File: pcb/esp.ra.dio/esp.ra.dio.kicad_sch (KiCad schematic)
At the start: 26 parts, among them J1 A, J10 UART, J2 B, J3 C, J4 D, J5 START, J6 SELECT, J7 JOY, J8 USB_B_Micro, J9 BATTERY, SW1 RESET, SW2 POWER, SW3 BOOT, U2 ESP32-C3-WROOM-02, U3 TLV75533PDBV

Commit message: Routing checkpoint
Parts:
- C1, C2, C3: footprint (none) -> Capacitor_SMD:C_0805_2012Metric_Pad1.18x1.45mm_HandSolder
- H1, H2, H3, H4: footprint (none) -> MountingHole:MountingHole_2.2mm_M2
- J10: footprint (none) -> Connector_PinHeader_2.54mm:PinHeader_1x04_P2.54mm_Vertical
- J8: footprint Connector_USB:USB_Micro-B_Amphenol_10118193-0001LF_Horizontal -> Connector_USB:USB_Micro-AB_Molex_47590-0001
- R1, R2, R3: footprint (none) -> Resistor_SMD:R_0805_2012Metric_Pad1.20x1.40mm_HandSolder
- SW1, SW3: footprint (none) -> Button_Switch_SMD:SW_SPST_PTS810
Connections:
- net GND: now also SW1.2; no longer SW1.1
- net VBAT: now also D2.1; no longer D2.2
- net VBUS: now also D2.2; no longer D2.1
- net VIN: now reaches SW2.2 (B), U3.1 (IN), U3.3 (EN)
- net at C3.2, R3.1: now also SW1.1; no longer SW1.2
- net VBATBUS: now reaches D2.3, SW2.3 (C)
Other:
- title: NG2040 Controller -> ESP.Ra.Dio BTLE Joystick
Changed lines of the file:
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@@
 	(paper "A4")
 	(title_block
-		(title "NG2040 Controller")
-		(date "2024-09-05")
-		(rev "4")
+		(title "ESP.Ra.Dio BTLE Joystick")
+		(date "2026-03-07")
+		(rev "2")
 		(company "@partlyhuman")
 	)
@@
 	(wire
 		(pts
+			(xy 57.15 26.67) (xy 67.31 26.67)
+		)
+		(stroke
+			(width 0)
+			(type default)
+		)
+	)
+	(wire
+		(pts
 			(xy 36.83 77.47) (xy 36.83 83.82)
 		)
@@
 	(wire
 		(pts
-			(xy 57.15 26.67) (xy 67.31 26.67)
-		)
-		(stroke
-			(width 0)
-			(type default)
-		)
-	)
-	(wire
-		(pts
 			(xy 110.49 45.72) (xy 110.49 48.26)
 		)
@@
 		)
 	)
+	(label "VIN"
+		(at 72.39 38.1 0)
+		(effects
+			(font
+				(size 1.27 1.27)
+			)
+			(justify left bottom)
+		)
+	)
 	(label "VBAT"
-		(at 67.31 26.67 180)
+		(at 57.15 26.67 0)
 		(effects
 			(font
 				(size 1.27 1.27)
 			)
-			(justify right bottom)
+			(justify left bottom)
 		)
 	)
@@
 		)
 	)
+	(label "VBATBUS"
+		(at 62.23 35.56 180)
+		(effects
+			(font
+				(size 1.27 1.27)
+			)
+			(justify right bottom)
+		)
+	)
 	(label "DU"
 		(at 154.94 91.44 180)
@@
 			)
 		)
-		(property "Footprint" ""
+		(property "Footprint" "Capacitor_SMD:C_0805_2012Metric_Pad1.18x1.45mm_HandSolder"
 			(at 67.31 67.31 0)
 			(effects
@@
 		(lib_id "Switch:SW_Push")
 		(at 67.31 63.5 0)
+		(mirror y)
 		(unit 1)
 		(exclude_from_sim no)
@@
 		(on_board yes)
 		(dnp no)
-		(fields_autoplaced yes)
 		(property "Reference" "SW1"
 			(at 67.31 55.88 0)
@@
 			)
 		)
-		(property "Footprint" ""
+		(property "Footprint" "Button_Switch_SMD:SW_SPST_PTS810"
 			(at 67.31 58.42 0)
 			(effects
@@
 			)
 		)
-		(property "Footprint" ""
+		(property "Footprint" "MountingHole:MountingHole_2.2mm_M2"
 			(at 265.43 20.32 0)
 			(effects
@@
 			)
 		)
-		(property "Footprint" ""
+		(property "Footprint" "Capacitor_SMD:C_0805_2012Metric_Pad1.18x1.45mm_HandSolder"
 			(at 104.14 43.18 0)
 			(effects
@@
 			)
 		)
-		(property "Footprint" "Connector_USB:USB_Micro-B_Amphenol_10118193-0001LF_Horizontal"
+		(property "Footprint" "Connector_USB:USB_Micro-AB_Molex_47590-0001"
 			(at 29.21 33.02 0)
 			(effects
@@
 			)
 		)
-		(property "Footprint" ""
+		(property "Footprint" "Capacitor_SMD:C_0805_2012Metric_Pad1.18x1.45mm_HandSolder"
 			(at 110.49 43.18 0)
 			(effects
@@
 			)
 		)
-		(property "Footprint" ""
+		(property "Footprint" "Resistor_SMD:R_0805_2012Metric_Pad1.20x1.40mm_HandSolder"
 			(at 157.48 71.12 0)
 			(effects
@@
 			)
 		)
-		(property "Footprint" ""
+		(property "Footprint" "MountingHole:MountingHole_2.2mm_M2"
 			(at 265.43 39.37 0)
 			(effects
@@
 		(lib_id "Diode:BAT54C")
 		(at 49.53 26.67 0)
+		(mirror y)
 		(unit 1)
 		(exclude_from_sim no)
@@
 		)
 		(property "Footprint" "Package_TO_SOT_SMD:SOT-23"
-			(at 51.435 23.495 0)
+			(at 47.625 23.495 0)
 			(effects
 				(font
@@
 		)
 		(property "Datasheet" "http://www.diodes.com/_files/datasheets/ds11005.pdf"
-			(at 47.498 26.67 0)
+			(at 51.562 26.67 0)
 			(effects
 				(font
@@
 			)
 		)
-		(property "Footprint" ""
+		(property "Footprint" "Resistor_SMD:R_0805_2012Metric_Pad1.20x1.40mm_HandSolder"
 			(at 157.48 73.66 0)
 			(effects
@@
 			)
 		)
-		(property "Footprint" ""
+		(property "Footprint" "MountingHole:MountingHole_2.2mm_M2"
 			(at 265.43 26.67 0)
 			(effects
@@
 			)
 		)
-		(property "Footprint" ""
+		(property "Footprint" "MountingHole:MountingHole_2.2mm_M2"
 			(at 265.43 33.02 0)
 			(effects
@@
 			)
 		)
-		(property "Footprint" ""
+		(property "Footprint" "Resistor_SMD:R_0805_2012Metric_Pad1.20x1.40mm_HandSolder"
 			(at 78.74 63.5 0)
 			(effects
@@
 			)
 		)
-		(property "Footprint" ""
+		(property "Footprint" "Connector_PinHeader_2.54mm:PinHeader_1x04_P2.54mm_Vertical"
 			(at 165.1 60.96 0)
 			(effects
@@
 		(on_board yes)
 		(dnp no)
-		(fields_autoplaced yes)
 		(property "Reference" "SW3"
 			(at 165.1 88.9 0)
@@
 			)
 		)
-		(property "Footprint" ""
+		(property "Footprint" "Button_Switch_SMD:SW_SPST_PTS810"
 			(at 165.1 91.44 0)
 			(effects

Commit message: Routing checkpoint
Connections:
- net BC: now also U2.10 (GPIO10); no longer U2.7 (GPIO8)
- net BD: now also U2.7 (GPIO8); no longer U2.10 (GPIO10)
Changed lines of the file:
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@@
 		)
 	)
-	(label "BD"
+	(label "BC"
 		(at 154.94 99.06 180)
 		(effects
@@
 		)
 	)
-	(label "BC"
+	(label "BD"
 		(at 154.94 93.98 180)
 		(effects

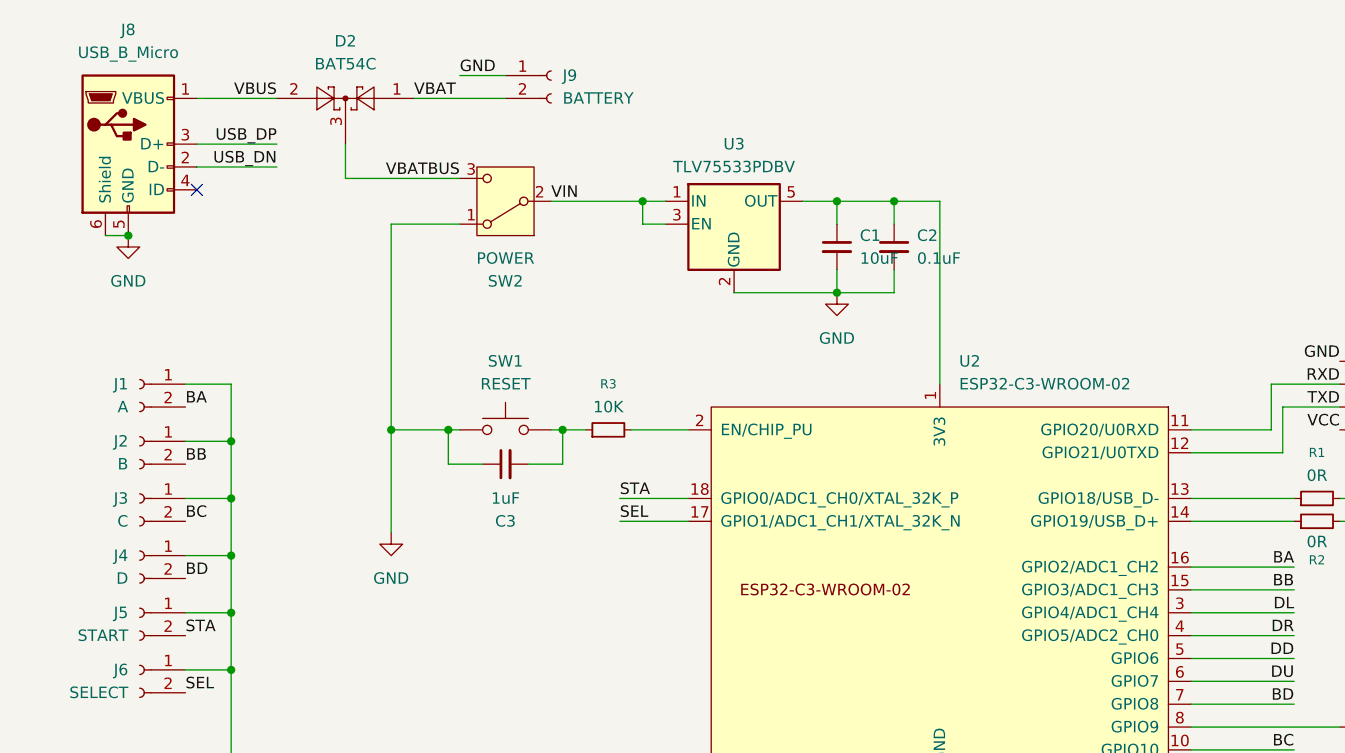
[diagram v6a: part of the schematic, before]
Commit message: Fix EN needs pullup
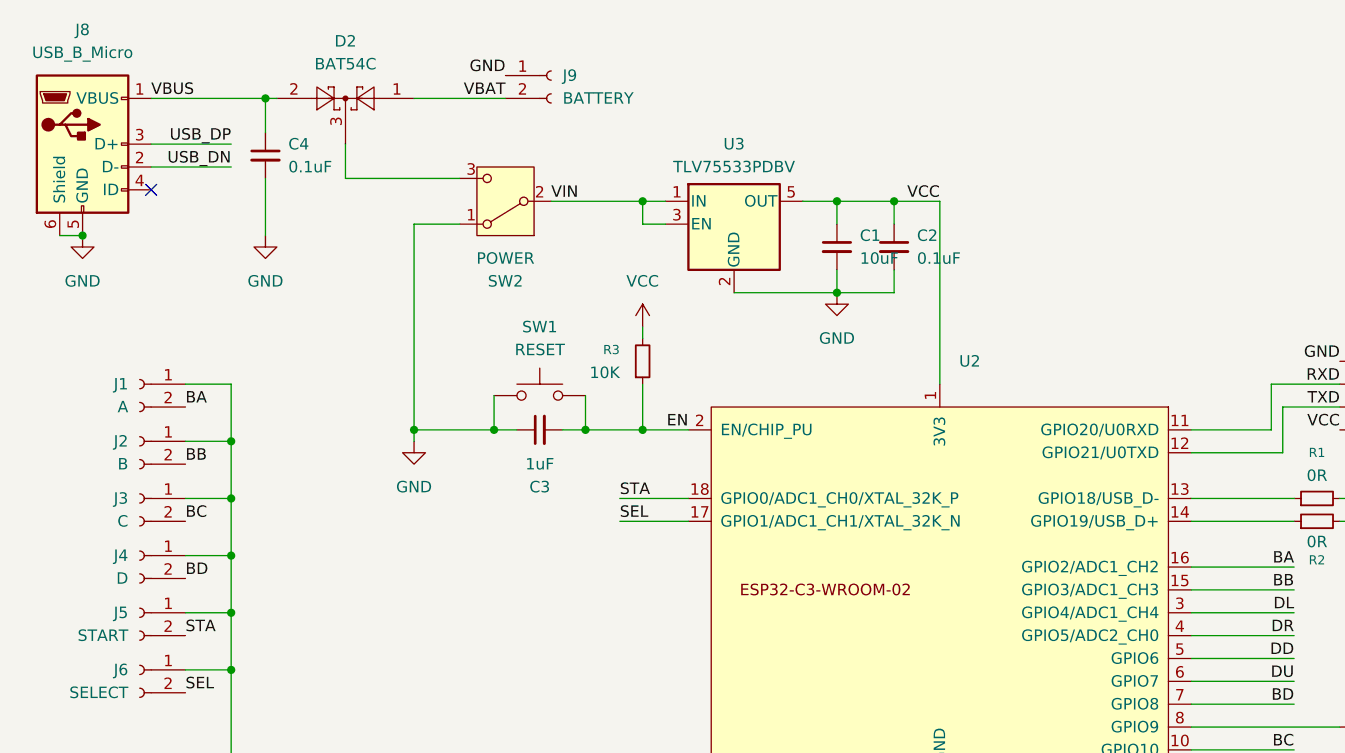
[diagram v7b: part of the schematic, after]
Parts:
- added C4: 0.1uF, Capacitor_SMD:C_0805_2012Metric_Pad1.18x1.45mm_HandSolder, symbol Device:C_Small
- U2: value ESP32-C3-WROOM-02 -> VCC
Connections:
- net GND: now also C4.2
- net VBUS: now also C4.1
- net VCC: now also C1.1, C2.1, R3.2, U2.1 (3V3), U3.5 (OUT)
- net EN: now reaches C3.2, R3.1, SW1.1
- net EN: now also U2.2 (EN/CHIP_PU)
- net VBATBUS: no longer names the net of D2.3, SW2.3 (C)
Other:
- moved on the sheet: C3, J8, R3, SW1

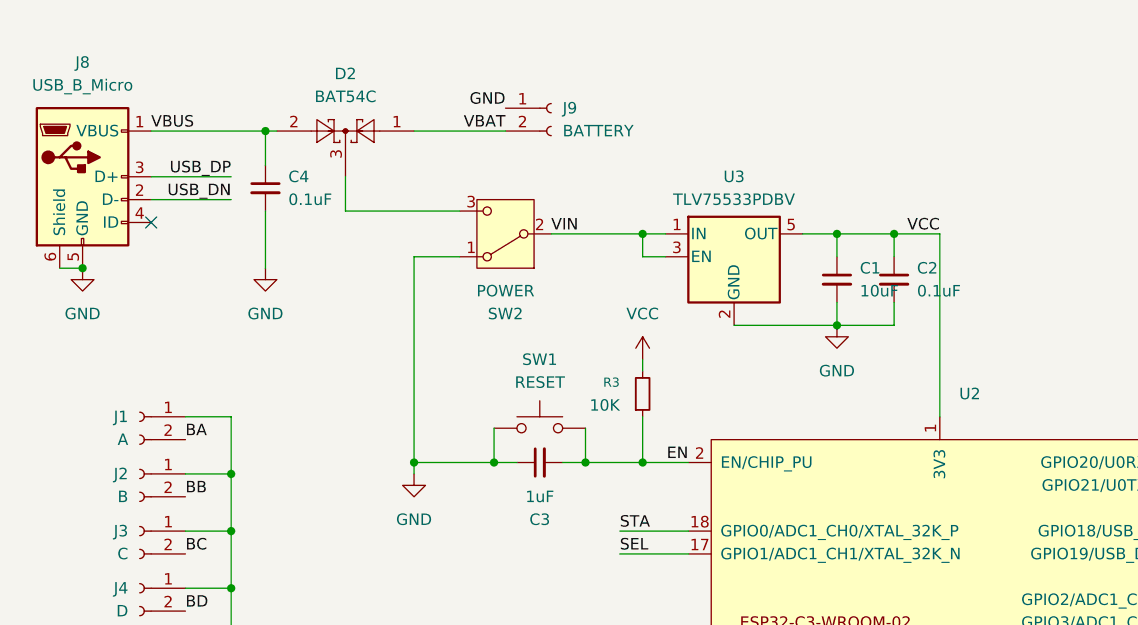
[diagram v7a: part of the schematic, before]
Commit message: Removes USB power, diode drop would have eaten into battery life too much
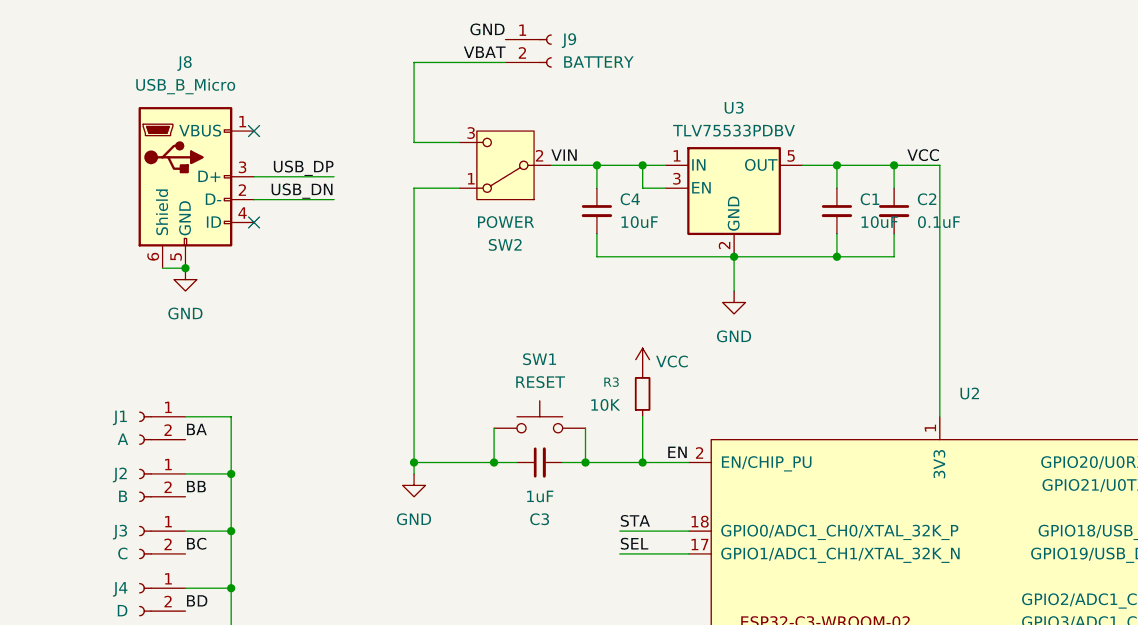
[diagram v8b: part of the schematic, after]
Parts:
- removed D2: BAT54C, Package_TO_SOT_SMD:SOT-23, symbol Diode:BAT54C
- C4: value 0.1uF -> 10uF
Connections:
- net VBAT: now also SW2.3 (C)
- net VIN: now also C4.1
- net VBUS: no longer names the net of J8.1 (VBUS)
- net VBUS: no longer C4.1
- no-connect marks 1 -> 2
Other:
- moved on the sheet: C1, C2, J8, J9, SW2, U3
